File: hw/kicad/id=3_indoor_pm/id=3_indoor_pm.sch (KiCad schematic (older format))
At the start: 74 parts, among them IC1 LPS22HB, IC2 24AA02T-I_OT, IC3 SHTC1, IC4 LM3671MF-1.8_NOPB, IC5 SGP30-2.5k, IC6 24AA02T-I_OT, IC7 SN74AUP1T17DCKR, IC8 nRF52840-QIAA-T, J1 HDR_2x2.54mm, J2 53047-0810, Q1 NMOS_DGS, Q2 NMOS_DGS, Y1 32MHZ, Y2 32.768K

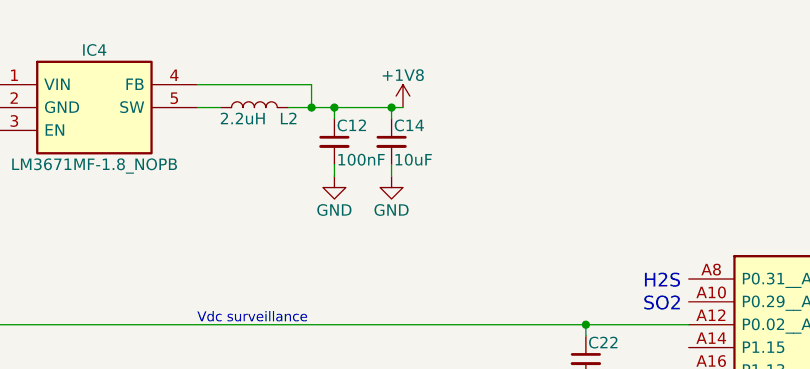
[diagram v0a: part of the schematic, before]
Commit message: Datasheets added Schematic for outdoor PM extended
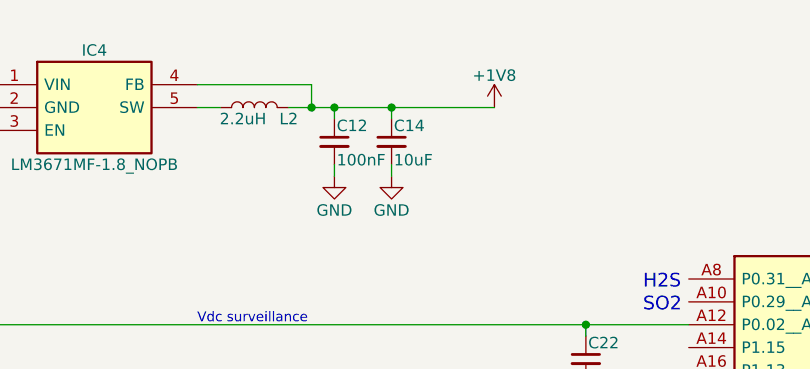
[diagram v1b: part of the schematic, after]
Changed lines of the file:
@@
 L +1V8 #PWR33
 U 1 1 5A747707
-P 4700 900
-F 0 "#PWR33" H 4700 750 50  0001 C CNN
-F 1 "+1V8" H 4700 1040 50  0000 C CNN
-F 2 "" H 4700 900 50  0001 C CNN
-F 3 "" H 4700 900 50  0001 C CNN
-	1    4700 900
+P 5100 900
+F 0 "#PWR33" H 5100 750 50  0001 C CNN
+F 1 "+1V8" H 5100 1040 50  0000 C CNN
+F 2 "" H 5100 900 50  0001 C CNN
+F 3 "" H 5100 900 50  0001 C CNN
+	1    5100 900
 	1    0    0    -1
 $EndComp
@@
 Wire Wire Line
 	3800 900  3900 900
-Wire Wire Line
-	4200 900  4700 900
 Wire Wire Line
 	4300 900  4300 800
@@
 Text Label 3300 4350 0    60   ~ 0
 SCL
+Wire Wire Line
+	5100 900  4200 900
 $EndSCHEMATC

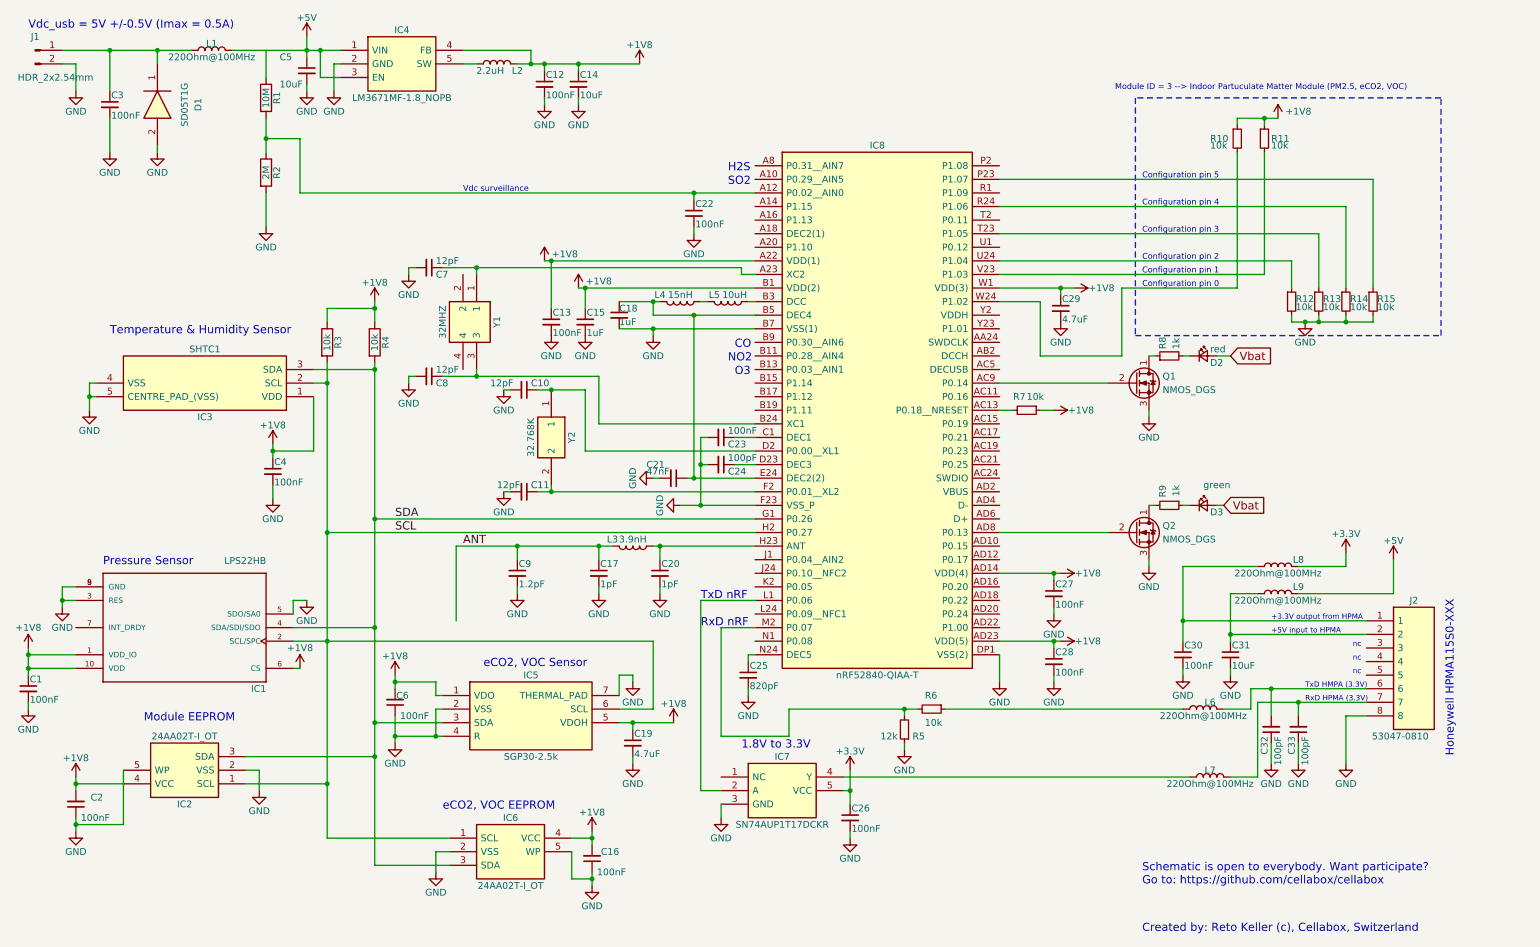
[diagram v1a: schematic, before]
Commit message: Updated schematics: battery surveillance.
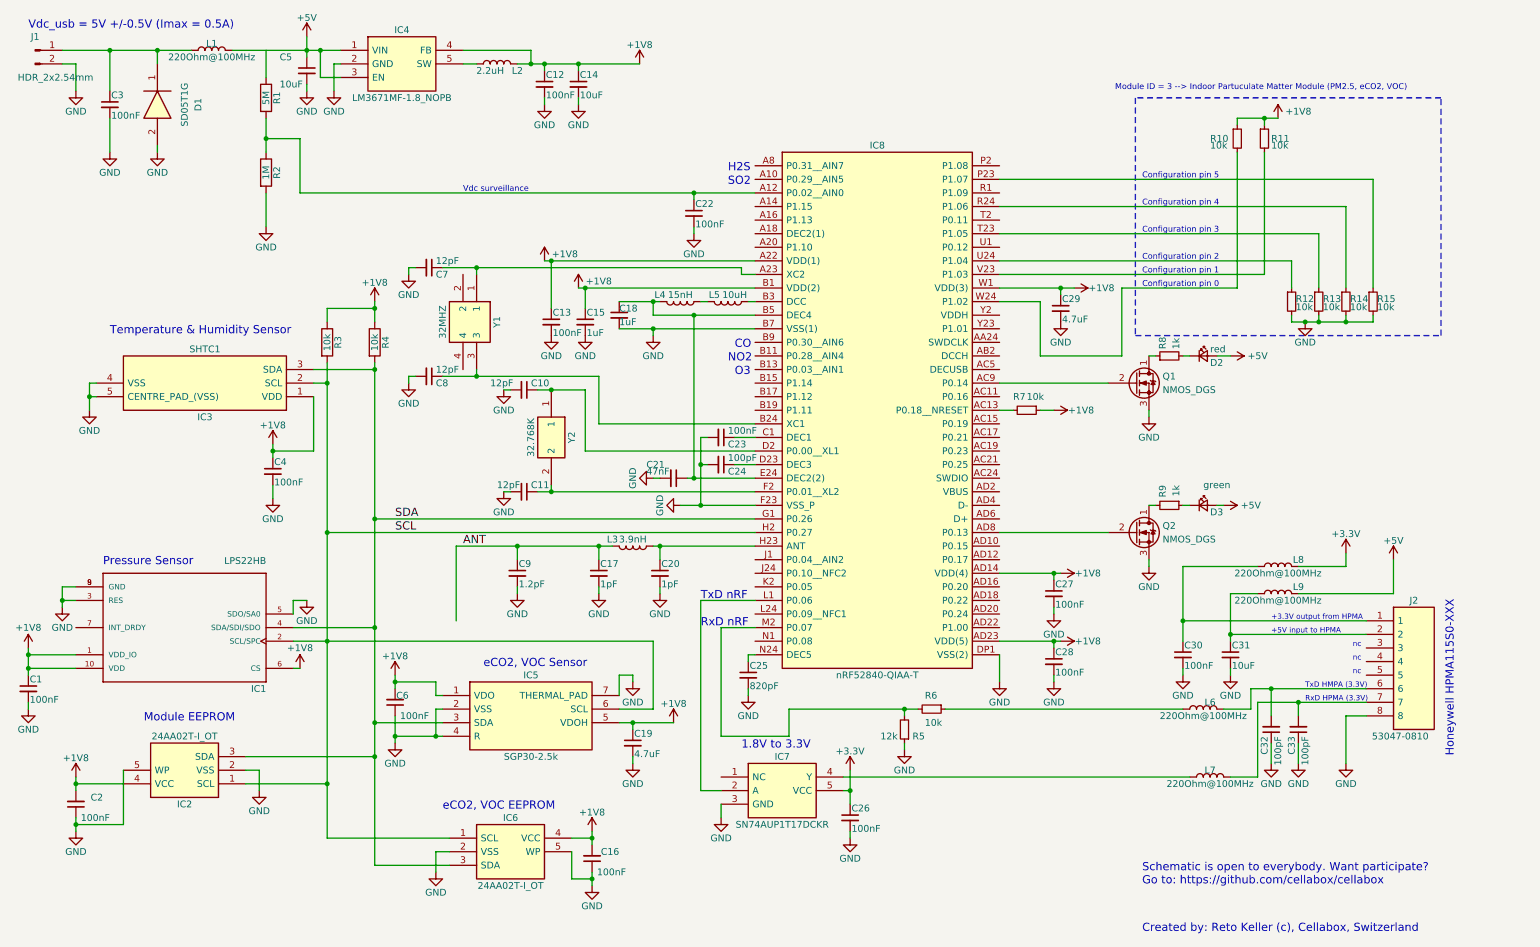
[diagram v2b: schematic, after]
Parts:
- R1: value 10M -> 5M
- R2: value 2M -> 1M
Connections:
- net Vbat is gone; now on net +5V: D2.2 (A), D3.2 (A)
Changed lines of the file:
@@
 P 2350 1150
 F 0 "R1" V 2430 1150 50  0000 C CNN
-F 1 "10M" V 2350 1150 50  0000 C CNN
+F 1 "5M" V 2350 1150 50  0000 C CNN
 F 2 "" V 2280 1150 50  0001 C CNN
 F 3 "" H 2350 1150 50  0001 C CNN
@@
 P 2350 1700
 F 0 "R2" V 2430 1700 50  0000 C CNN
-F 1 "2M" V 2350 1700 50  0000 C CNN
+F 1 "1M" V 2350 1700 50  0000 C CNN
 F 2 "" V 2280 1700 50  0001 C CNN
 F 3 "" H 2350 1700 50  0001 C CNN
@@
 	1    0    0    -1
 $EndComp
-Text GLabel 9400 4150 2    60   Input ~ 0
-Vbat
 $Comp
 L GND #PWR59
@@
 	1    0    0    -1
 $EndComp
-Text GLabel 9450 3050 2    60   Input ~ 0
-Vbat
 $Comp
 L LPS22HB IC1
@@
 Wire Wire Line
 	5100 900  4200 900
+$Comp
+L +5V #PWR?
+U 1 1 5A7C1B42
+P 9450 3050
+F 0 "#PWR?" H 9450 2900 50  0001 C CNN
+F 1 "+5V" V 9450 3250 50  0000 C CNN
+F 2 "" H 9450 3050 50  0001 C CNN
+F 3 "" H 9450 3050 50  0001 C CNN
+	1    9450 3050
+	0    1    1    0
+$EndComp
+$Comp
+L +5V #PWR?
+U 1 1 5A7C1E4A
+P 9400 4150
+F 0 "#PWR?" H 9400 4000 50  0001 C CNN
+F 1 "+5V" V 9400 4350 50  0000 C CNN
+F 2 "" H 9400 4150 50  0001 C CNN
+F 3 "" H 9400 4150 50  0001 C CNN
+	1    9400 4150
+	0    1    1    0
+$EndComp
 $EndSCHEMATC
